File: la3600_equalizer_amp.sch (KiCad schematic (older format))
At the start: 53 parts, among them J1 JACK_TRS_3PINS, J2 JACK_TRS_3PINS, U1 LA3600, U2 LA3600, U3 LM386, U4 LM386

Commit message: rename project files (lm -> la oops). add some values to components in Eeschema
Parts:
- C30, C31: value CP1_Small -> 1uF
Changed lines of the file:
@@
 EESchema Schematic File Version 4
-LIBS:lm3600_equalizer_amp-cache
 EELAYER 26 0
 EELAYER END
@@
 U 1 1 5B7A7DF3
 P 9100 2250
-F 0 "U3" H 9441 2296 50  0000 L CNN
-F 1 "LM386" H 9441 2205 50  0000 L CNN
+F 0 "U3" H 9350 2500 50  0000 L CNN
+F 1 "LM386" H 9300 2400 50  0000 L CNN
 F 2 "" H 9200 2350 50  0001 C CNN
 F 3 "http://www.ti.com/lit/ds/symlink/lm386.pdf" H 9300 2450 50  0001 C CNN
@@
 P 7100 2300
 F 0 "C30" V 7328 2300 50  0000 C CNN
-F 1 "CP1_Small" V 7237 2300 50  0000 C CNN
+F 1 "1uF" V 7237 2300 50  0000 C CNN
 F 2 "" H 7100 2300 50  0001 C CNN
 F 3 "~" H 7100 2300 50  0001 C CNN
@@
 P 7400 5150
 F 0 "C31" V 7628 5150 50  0000 C CNN
-F 1 "CP1_Small" V 7537 5150 50  0000 C CNN
+F 1 "1uF" V 7537 5150 50  0000 C CNN
 F 2 "" H 7400 5150 50  0001 C CNN
 F 3 "~" H 7400 5150 50  0001 C CNN
@@
 U 1 1 5B99DB61
 P 9100 4350
-F 0 "U4" H 9441 4396 50  0000 L CNN
-F 1 "LM386" H 9441 4305 50  0000 L CNN
+F 0 "U4" H 9300 4600 50  0000 L CNN
+F 1 "LM386" H 9200 4500 50  0000 L CNN
 F 2 "" H 9200 4450 50  0001 C CNN
 F 3 "http://www.ti.com/lit/ds/symlink/lm386.pdf" H 9300 4550 50  0001 C CNN

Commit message: add usb b type connector for powering the device. assign footprints
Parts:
- added J3: USB_B, Connector_USB:USB_B_OST_USB-B1HSxx_Horizontal, symbol Connector:USB_B
- 22K1, 22K2, 22K3, 22K4, 22K5, 22K6: footprint (none) -> Potentiometer_THT:Potentiometer_Alps_RK163_Dual_Horizontal
- C1, C12, C2, C20, C22, C24, C28, C3, C30, C31, C4: footprint (none) -> Capacitor_THT:CP_Radial_D5.0mm_P2.50mm
- C10, C11, C13, C14, C15, C16, C17, C18, C19, C21, C23, C25, C26, C27, C29, C32, C33, C34, C35, C5, C6, C7, C8, C9: footprint (none) -> Capacitor_THT:C_Disc_D3.0mm_W2.0mm_P2.50mm
- C36, C37: footprint (none) -> Capacitor_THT:CP_Radial_D10.0mm_P5.00mm
- R1, R2, R3, R4: footprint (none) -> Resistor_THT:R_Axial_DIN0207_L6.3mm_D2.5mm_P10.16mm_Horizontal
- U1, U2: footprint (none) -> Package_DIP:DIP-16_W7.62mm_Socket
- U3: footprint (none) -> Package_DIP:DIP-6_W7.62mm_Socket
- U4: footprint (none) -> Package_DIP:DIP-8_W7.62mm_Socket
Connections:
- wire segments 216 -> 221
- no-connect marks 6 -> 9

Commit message: initial pcb layout
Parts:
- U3: footprint Package_DIP:DIP-6_W7.62mm_Socket -> Package_DIP:DIP-8_W7.62mm_Socket
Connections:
- wire segments 221 -> 223
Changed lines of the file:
@@
 EESchema Schematic File Version 4
+LIBS:la3600_equalizer_amp-cache
 EELAYER 26 0
 EELAYER END
@@
 F 0 "U3" H 9350 2500 50  0000 L CNN
 F 1 "LM386" H 9300 2400 50  0000 L CNN
-F 2 "Package_DIP:DIP-6_W7.62mm_Socket" H 9200 2350 50  0001 C CNN
+F 2 "Package_DIP:DIP-8_W7.62mm_Socket" H 9200 2350 50  0001 C CNN
 F 3 "http://www.ti.com/lit/ds/symlink/lm386.pdf" H 9300 2450 50  0001 C CNN
 	1    9100 2250
@@
 	1400 2050 1400 800
 Connection ~ 1400 800
+Text GLabel 6500 2050 2    50   Input ~ 0
+GND
+Text GLabel 6800 4900 2    50   Input ~ 0
+GND
+Wire Wire Line
+	6450 2050 6500 2050
+Wire Wire Line
+	6750 4900 6800 4900
 $EndSCHEMATC

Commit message: kicad 5 modifications
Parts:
- U3, U4: symbol Amplifier_Audio:LM386 -> la3600_equalizer_amp-rescue:LM386-Amplifier_Audio
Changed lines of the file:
@@
 $EndComp
 $Comp
-L Amplifier_Audio:LM386 U3
+L la3600_equalizer_amp-rescue:LM386-Amplifier_Audio U3
 U 1 1 5B7A7DF3
 P 9100 2250
@@
 Connection ~ 9550 2250
 $Comp
-L Amplifier_Audio:LM386 U4
+L la3600_equalizer_amp-rescue:LM386-Amplifier_Audio U4
 U 1 1 5B99DB61
 P 9100 4350

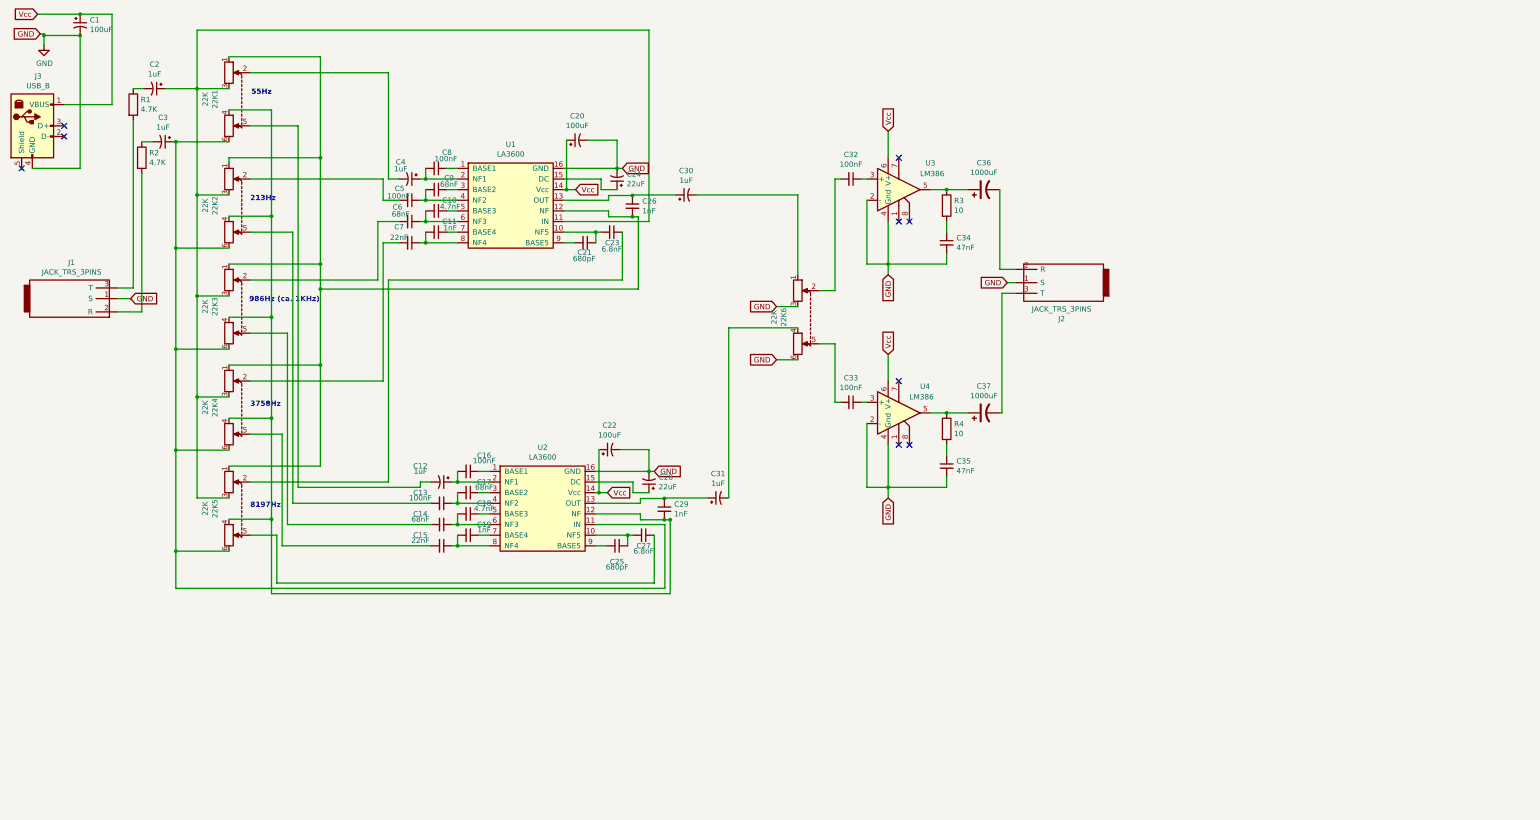
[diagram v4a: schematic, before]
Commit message: replace the audio amplifier part of the circuit with a new one based on NE5532 and BD139/BD140 output stage
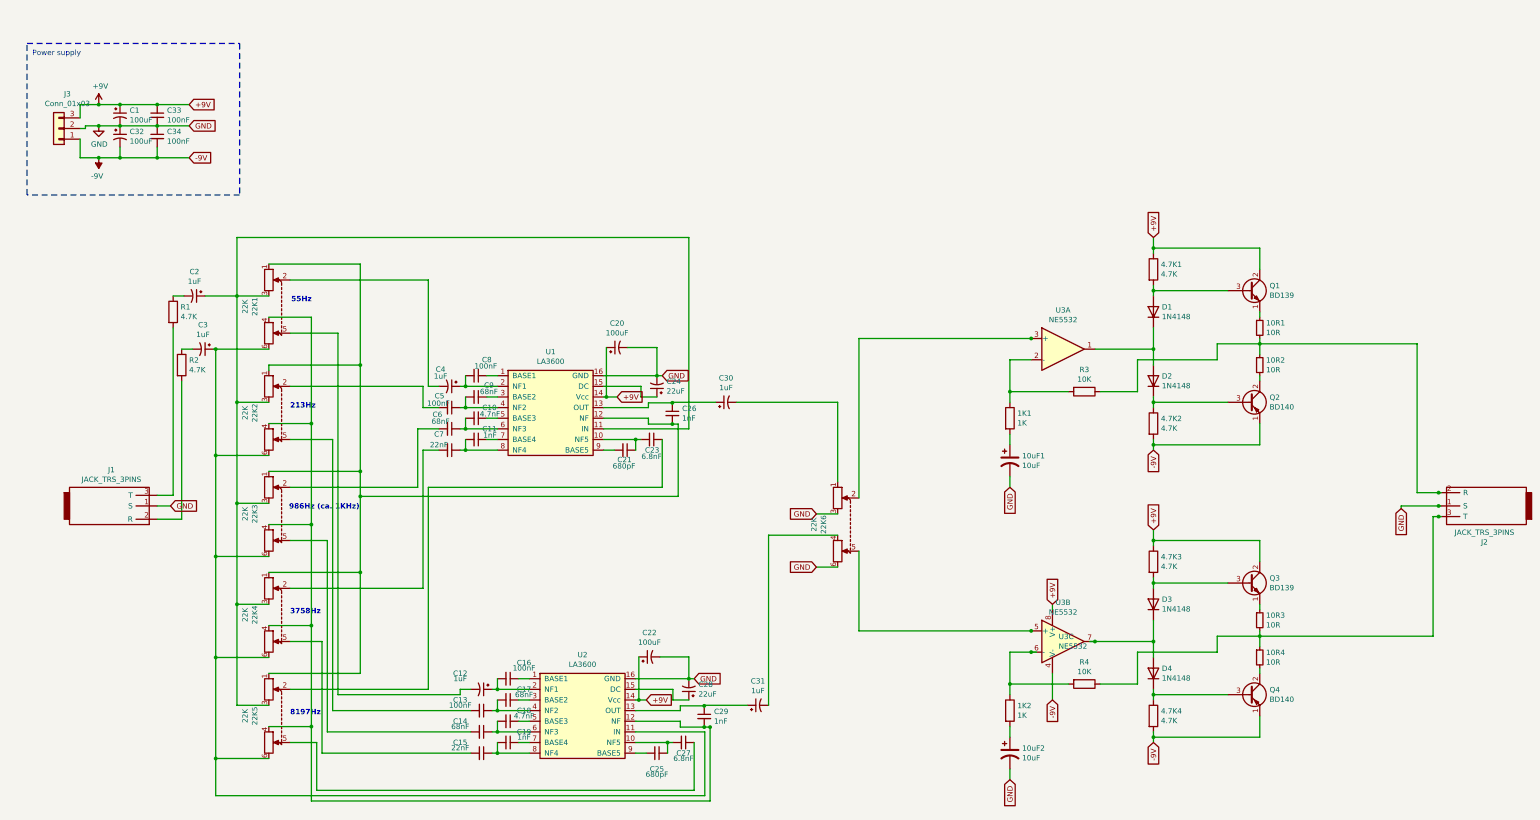
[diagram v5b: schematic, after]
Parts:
- removed C32: 100nF, Capacitor_THT:C_Disc_D3.0mm_W2.0mm_P2.50mm, symbol Device:C_Small
- removed C35: 47nF, Capacitor_THT:C_Disc_D3.0mm_W2.0mm_P2.50mm, symbol Device:C_Small
- removed C36, C37: 1000uF, Capacitor_THT:CP_Radial_D10.0mm_P5.00mm, symbol Device:CP1
- removed J3: USB_B, Connector_USB:USB_B_OST_USB-B1HSxx_Horizontal, symbol Connector:USB_B
- removed U3, U4: LM386, Package_DIP:DIP-8_W7.62mm_Socket, symbol la3600_equalizer_amp-rescue:LM386-Amplifier_Audio
- added 10R1, 10R2, 10R3, 10R4: 10R, Resistor_THT:R_Axial_DIN0207_L6.3mm_D2.5mm_P10.16mm_Horizontal, symbol Device:R_Small
- added 10uF1, 10uF2: 10uF, Capacitor_THT:CP_Radial_D5.0mm_P2.50mm, symbol Device:CP1
- added 1K1, 1K2: 1K, Resistor_THT:R_Axial_DIN0207_L6.3mm_D2.5mm_P10.16mm_Horizontal, symbol Device:R
- added 4.7K1, 4.7K2, 4.7K3, 4.7K4: 4.7K, Resistor_THT:R_Axial_DIN0207_L6.3mm_D2.5mm_P10.16mm_Horizontal, symbol Device:R
- added C32: 100uF, Capacitor_THT:CP_Radial_D5.0mm_P2.50mm, symbol Device:CP1_Small
- added D1, D2, D3, D4: 1N4148, Diode_THT:D_DO-35_SOD27_P7.62mm_Horizontal, symbol Diode:1N4148
- added J3: Conn_01x03, Connector_PinHeader_2.54mm:PinHeader_1x03_P2.54mm_Vertical, symbol Connector_Generic:Conn_01x03
- added Q1, Q3: BD139, Package_TO_SOT_THT:TO-126-3_Vertical, symbol Transistor_BJT:BD139
- added Q2, Q4: BD140, Package_TO_SOT_THT:TO-126-3_Vertical, symbol Transistor_BJT:BD140
- added U3: NE5532, Package_DIP:DIP-8_W7.62mm_Socket, symbol Amplifier_Operational:NE5532
- C34: value 47nF -> 100nF
- R3, R4: value 10 -> 10K
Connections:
- net labels added: +9V, -9V
- net labels removed: Vcc
- wire segments 223 -> 282
- no-connect marks 9 -> 0
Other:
- note added: "Power supply"
- moved on the sheet: 22K1, 22K2, 22K3, 22K4, 22K5, 22K6, C10, C11, C12, C13, C14, C15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
